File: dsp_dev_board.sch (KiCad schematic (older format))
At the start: 28 parts, among them J1 aux_mcu_power, J2 audio_in, J3 audio_out, J4 9v_jack, J5 input_jack, J6 output_jack, U1 TL072, U2 AMS1117-3.3, U6 AMS1117-1.8

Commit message: Add pull-up resistors for I2C
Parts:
- added R20, R21: 10k, Resistor_SMD:R_0603_1608Metric, symbol Device:R
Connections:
- net 3.3V: now also R20.2, R21.2
- net MCU/SCL: now also R21.1
- net MCU/SDA: now also R20.1
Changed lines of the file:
@@
 	6800 4650 7100 4650
 Wire Wire Line
-	6450 5550 9300 5550
+	6450 5550 8550 5550
 Wire Wire Line
-	6450 5650 9300 5650
+	6450 5650 8850 5650
 Wire Wire Line
 	6450 5750 9300 5750
@@
 	4350 2400 4200 2400
 Connection ~ 4200 2400
+Wire Wire Line
+	8550 5500 8550 5550
+Connection ~ 8550 5550
+Wire Wire Line
+	8550 5550 9300 5550
+$Comp
+L Device:R R20
+U 1 1 608A7F3C
+P 8550 5350
+F 0 "R20" H 8400 5300 50  0000 C CNN
+F 1 "10k" H 8400 5400 50  0000 C CNN
+F 2 "Resistor_SMD:R_0603_1608Metric" V 8480 5350 50  0001 C CNN
+F 3 "~" H 8550 5350 50  0001 C CNN
+	1    8550 5350
+	-1   0    0    1
+$EndComp
+$Comp
+L Device:R R21
+U 1 1 608A8BFD
+P 8850 5350
+F 0 "R21" H 8700 5300 50  0000 C CNN
+F 1 "10k" H 8700 5400 50  0000 C CNN
+F 2 "Resistor_SMD:R_0603_1608Metric" V 8780 5350 50  0001 C CNN
+F 3 "~" H 8850 5350 50  0001 C CNN
+	1    8850 5350
+	-1   0    0    1
+$EndComp
+Wire Wire Line
+	8850 5500 8850 5650
+Connection ~ 8850 5650
+Wire Wire Line
+	8850 5650 9300 5650
+Wire Wire Line
+	8850 5200 8850 5150
+Wire Wire Line
+	8850 5150 8550 5150
+Wire Wire Line
+	8550 5150 8550 5200
+Text GLabel 8400 5100 0    50   Input ~ 0
+3.3V
+Wire Wire Line
+	8400 5100 8550 5100
+Wire Wire Line
+	8550 5100 8550 5150
+Connection ~ 8550 5150
 $EndSCHEMATC

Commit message: "0.1u" -> "100n"; use 1206 10u for bulk decoupling
The 1206 size has a much better derating-vs-bias-voltage curve.
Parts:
- C1: value 0.1u -> 10u; footprint Capacitor_SMD:C_0603_1608Metric -> Capacitor_SMD:C_1206_3216Metric
- C36: footprint Capacitor_SMD:C_0603_1608Metric -> Capacitor_SMD:C_1206_3216Metric
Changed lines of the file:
@@
 P 2550 2650
 F 0 "C1" H 2665 2696 50  0000 L CNN
-F 1 "0.1u" H 2665 2605 50  0000 L CNN
-F 2 "Capacitor_SMD:C_0603_1608Metric" H 2588 2500 50  0001 C CNN
+F 1 "10u" H 2665 2605 50  0000 L CNN
+F 2 "Capacitor_SMD:C_1206_3216Metric" H 2588 2500 50  0001 C CNN
 F 3 "~" H 2550 2650 50  0001 C CNN
 	1    2550 2650
@@
 F 0 "C36" H 4315 2646 50  0000 L CNN
 F 1 "10u" H 4315 2555 50  0000 L CNN
-F 2 "Capacitor_SMD:C_0603_1608Metric" H 4238 2450 50  0001 C CNN
+F 2 "Capacitor_SMD:C_1206_3216Metric" H 4238 2450 50  0001 C CNN
 F 3 "~" H 4200 2600 50  0001 C CNN
 	1    4200 2600

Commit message: Add a 10u decoupling for the main 9V supply
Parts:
- added C37: 10u, Capacitor_SMD:C_1206_3216Metric, symbol Device:C
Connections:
- net 9V: now also C37.1
- net GND: now also C37.2
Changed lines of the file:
@@
 $EndComp
 Wire Wire Line
-	3050 1400 2850 1400
+	3050 1400 2950 1400
 Wire Wire Line
 	2550 1400 2350 1400
@@
 	8550 5100 8550 5150
 Connection ~ 8550 5150
+$Comp
+L Device:C C37
+U 1 1 608FE6BA
+P 2950 1650
+F 0 "C37" H 3065 1696 50  0000 L CNN
+F 1 "10u" H 3065 1605 50  0000 L CNN
+F 2 "Capacitor_SMD:C_1206_3216Metric" H 2988 1500 50  0001 C CNN
+F 3 "~" H 2950 1650 50  0001 C CNN
+	1    2950 1650
+	1    0    0    -1
+$EndComp
+Wire Wire Line
+	2950 1400 2950 1500
+Connection ~ 2950 1400
+Wire Wire Line
+	2950 1400 2850 1400
+$Comp
+L power:GND #PWR0101
+U 1 1 609053CE
+P 2950 1850
+F 0 "#PWR0101" H 2950 1600 50  0001 C CNN
+F 1 "GND" H 2955 1677 50  0000 C CNN
+F 2 "" H 2950 1850 50  0001 C CNN
+F 3 "" H 2950 1850 50  0001 C CNN
+	1    2950 1850
+	1    0    0    -1
+$EndComp
+Wire Wire Line
+	2950 1800 2950 1850
 $EndSCHEMATC

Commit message: sch: add jumpers to select audio path
This way the unused codec's audio path won't be dangling as an antenna
picking up unnecessary noise on the analog side
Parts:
- added R? (x4): 0 DNP, Resistor_SMD:R_0603_1608Metric, symbol Device:R
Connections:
- net audio_in: now also R?.2, R?.2
- net audio_out: now also R?.1, R?.1
- new net Codec/audio_in: R?.1
- new net Codec/audio_out: R?.2
- new net TI Codec/audio_in: R?.1
- new net TI Codec/audio_out: R?.2
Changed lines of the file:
@@
 Wire Wire Line
 	10250 1800 9850 1800
-Text Label 6950 4450 2    50   ~ 0
+Text Label 6650 4450 2    50   ~ 0
 audio_in
 Wire Wire Line
@@
 Wire Wire Line
 	6750 3150 7050 3150
-Text Label 8150 4450 0    50   ~ 0
+Text Label 8450 4450 0    50   ~ 0
 audio_out
 Wire Wire Line
@@
 F11 "DOUT" O L 9300 4750 50
 $EndSheet
-Text Label 9150 4450 2    50   ~ 0
+Text Label 8950 4150 2    50   ~ 0
 audio_in
-Wire Wire Line
-	9150 4450 9300 4450
-Text Label 10600 4450 0    50   ~ 0
+Text Label 10800 4150 0    50   ~ 0
 audio_out
-Wire Wire Line
-	10600 4450 10450 4450
 Wire Wire Line
 	6800 5050 6800 5000
@@
 Wire Wire Line
 	2950 1800 2950 1850
+$Comp
+L Device:R R?
+U 1 1 607E529D
+P 6800 4450
+F 0 "R?" V 6593 4450 50  0000 C CNN
+F 1 "0 DNP" V 6684 4450 50  0000 C CNN
+F 2 "Resistor_SMD:R_0603_1608Metric" V 6730 4450 50  0001 C CNN
+F 3 "~" H 6800 4450 50  0001 C CNN
+	1    6800 4450
+	0    1    1    0
+$EndComp
+$Comp
+L Device:R R?
+U 1 1 607E8DDA
+P 8300 4450
+F 0 "R?" V 8093 4450 50  0000 C CNN
+F 1 "0 DNP" V 8184 4450 50  0000 C CNN
+F 2 "Resistor_SMD:R_0603_1608Metric" V 8230 4450 50  0001 C CNN
+F 3 "~" H 8300 4450 50  0001 C CNN
+	1    8300 4450
+	0    1    1    0
+$EndComp
+Wire Wire Line
+	9250 4450 9300 4450
+$Comp
+L Device:R R?
+U 1 1 607EA958
+P 9100 4150
+F 0 "R?" V 8893 4150 50  0000 C CNN
+F 1 "0 DNP" V 8984 4150 50  0000 C CNN
+F 2 "Resistor_SMD:R_0603_1608Metric" V 9030 4150 50  0001 C CNN
+F 3 "~" H 9100 4150 50  0001 C CNN
+	1    9100 4150
+	0    1    1    0
+$EndComp
+Wire Wire Line
+	9250 4150 9250 4450
+$Comp
+L Device:R R?
+U 1 1 607F9AAB
+P 10650 4150
+F 0 "R?" V 10443 4150 50  0000 C CNN
+F 1 "0 DNP" V 10534 4150 50  0000 C CNN
+F 2 "Resistor_SMD:R_0603_1608Metric" V 10580 4150 50  0001 C CNN
+F 3 "~" H 10650 4150 50  0001 C CNN
+	1    10650 4150
+	0    1    1    0
+$EndComp
+Wire Wire Line
+	10500 4150 10500 4450
+Wire Wire Line
+	10500 4450 10450 4450
 $EndSCHEMATC

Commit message: Annotate schematic symbols
I forgot to do this when I added the jumper resistors.
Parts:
- gave numbers to parts that had none: 4
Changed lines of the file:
@@
 	2950 1800 2950 1850
 $Comp
-L Device:R R?
+L Device:R R23
 U 1 1 607E529D
 P 6800 4450
-F 0 "R?" V 6593 4450 50  0000 C CNN
+F 0 "R23" V 6593 4450 50  0000 C CNN
 F 1 "0 DNP" V 6684 4450 50  0000 C CNN
 F 2 "Resistor_SMD:R_0603_1608Metric" V 6730 4450 50  0001 C CNN
@@
 $EndComp
 $Comp
-L Device:R R?
+L Device:R R24
 U 1 1 607E8DDA
 P 8300 4450
-F 0 "R?" V 8093 4450 50  0000 C CNN
+F 0 "R24" V 8093 4450 50  0000 C CNN
 F 1 "0 DNP" V 8184 4450 50  0000 C CNN
 F 2 "Resistor_SMD:R_0603_1608Metric" V 8230 4450 50  0001 C CNN
@@
 	9250 4450 9300 4450
 $Comp
-L Device:R R?
+L Device:R R25
 U 1 1 607EA958
 P 9100 4150
-F 0 "R?" V 8893 4150 50  0000 C CNN
+F 0 "R25" V 8893 4150 50  0000 C CNN
 F 1 "0 DNP" V 8984 4150 50  0000 C CNN
 F 2 "Resistor_SMD:R_0603_1608Metric" V 9030 4150 50  0001 C CNN
@@
 	9250 4150 9250 4450
 $Comp
-L Device:R R?
+L Device:R R26
 U 1 1 607F9AAB
 P 10650 4150
-F 0 "R?" V 10443 4150 50  0000 C CNN
+F 0 "R26" V 10443 4150 50  0000 C CNN
 F 1 "0 DNP" V 10534 4150 50  0000 C CNN
 F 2 "Resistor_SMD:R_0603_1608Metric" V 10580 4150 50  0001 C CNN

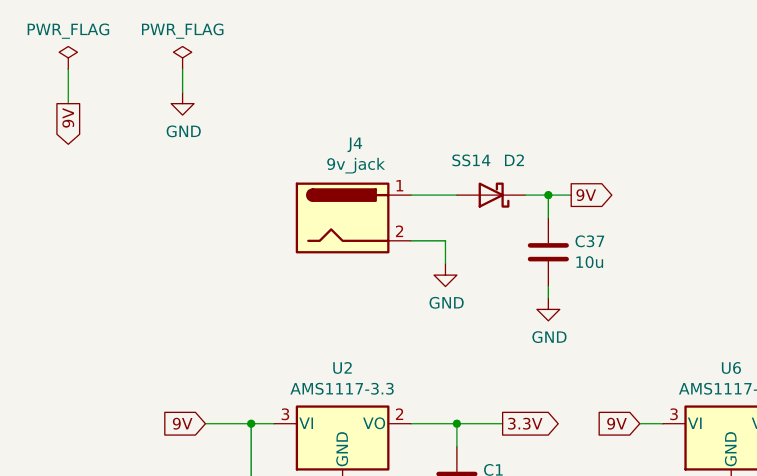
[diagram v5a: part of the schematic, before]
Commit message: power should be center-negative
And add attribution text to the PCB
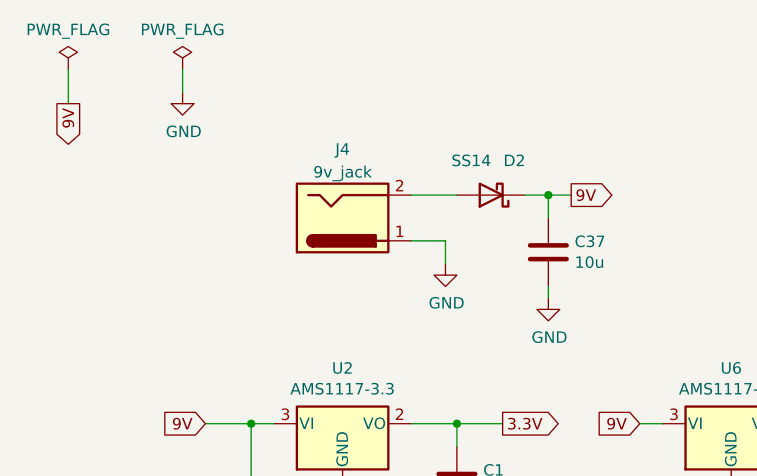
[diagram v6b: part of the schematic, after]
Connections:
- net GND: now also J4.1; no longer J4.2
- net at D2.2 (A): now also J4.2; no longer J4.1
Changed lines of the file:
@@
 U 1 1 60004038
 P 2050 1500
-F 0 "J4" H 2107 1825 50  0000 C CNN
-F 1 "9v_jack" H 2107 1734 50  0000 C CNN
+F 0 "J4" H 2050 1200 50  0000 C CNN
+F 1 "9v_jack" H 2050 1300 50  0000 C CNN
 F 2 "Connector_BarrelJack:BarrelJack_Horizontal" H 2100 1460 50  0001 C CNN
 F 3 "~" H 2100 1460 50  0001 C CNN
 	1    2050 1500
-	1    0    0    -1
+	1    0    0    1
 $EndComp
 Text GLabel 3050 1400 2    50   Output ~ 0
